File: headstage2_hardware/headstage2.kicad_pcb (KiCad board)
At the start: 6 copper layers, 113 parts, among them U1 OMNETICS_A79025, U10 TPS62410, U11 ABM10XTAL, U12 BF532-160, U13 NRF24L01, U14 MAX6711T, U15 SST25VF040B, U16 9x100, U17 ANTENNA, U18 9x100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

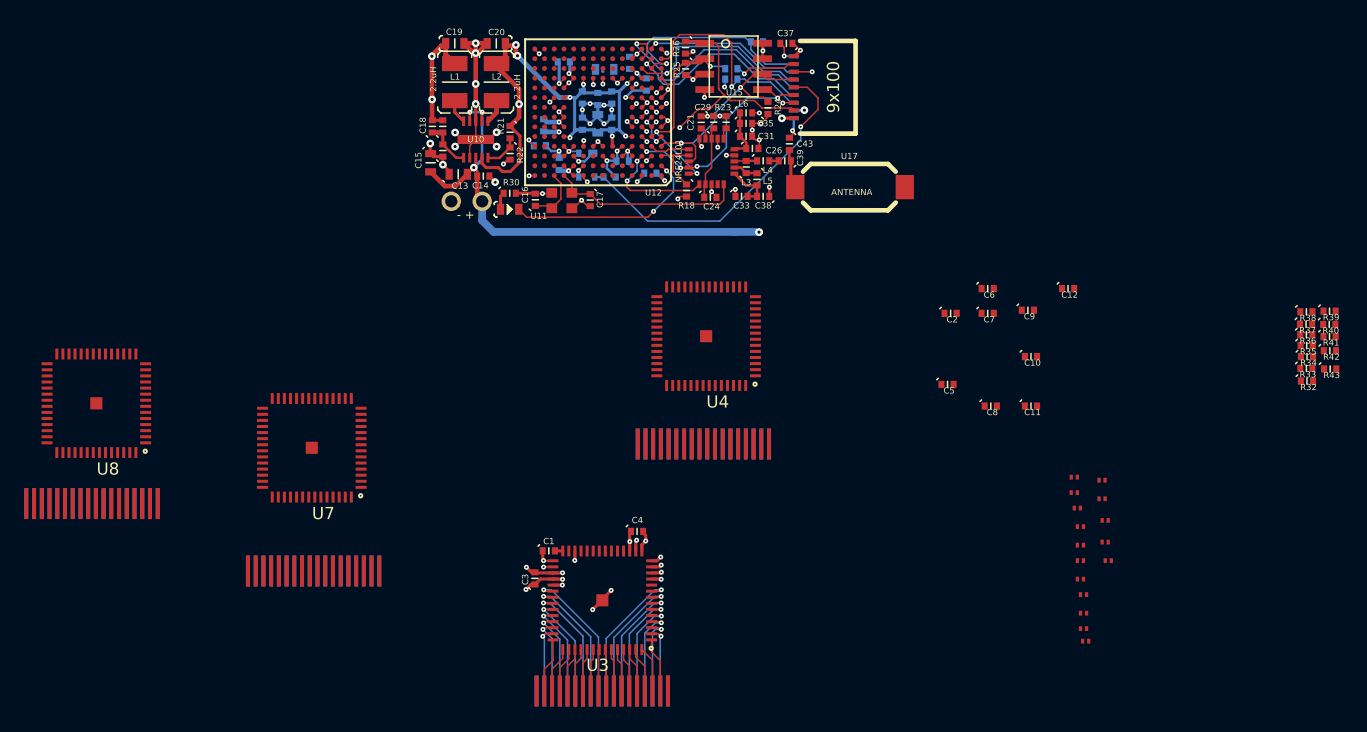
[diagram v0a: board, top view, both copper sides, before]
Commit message: Finished PCB layout, generated Gerber passed freedfm.com online check.
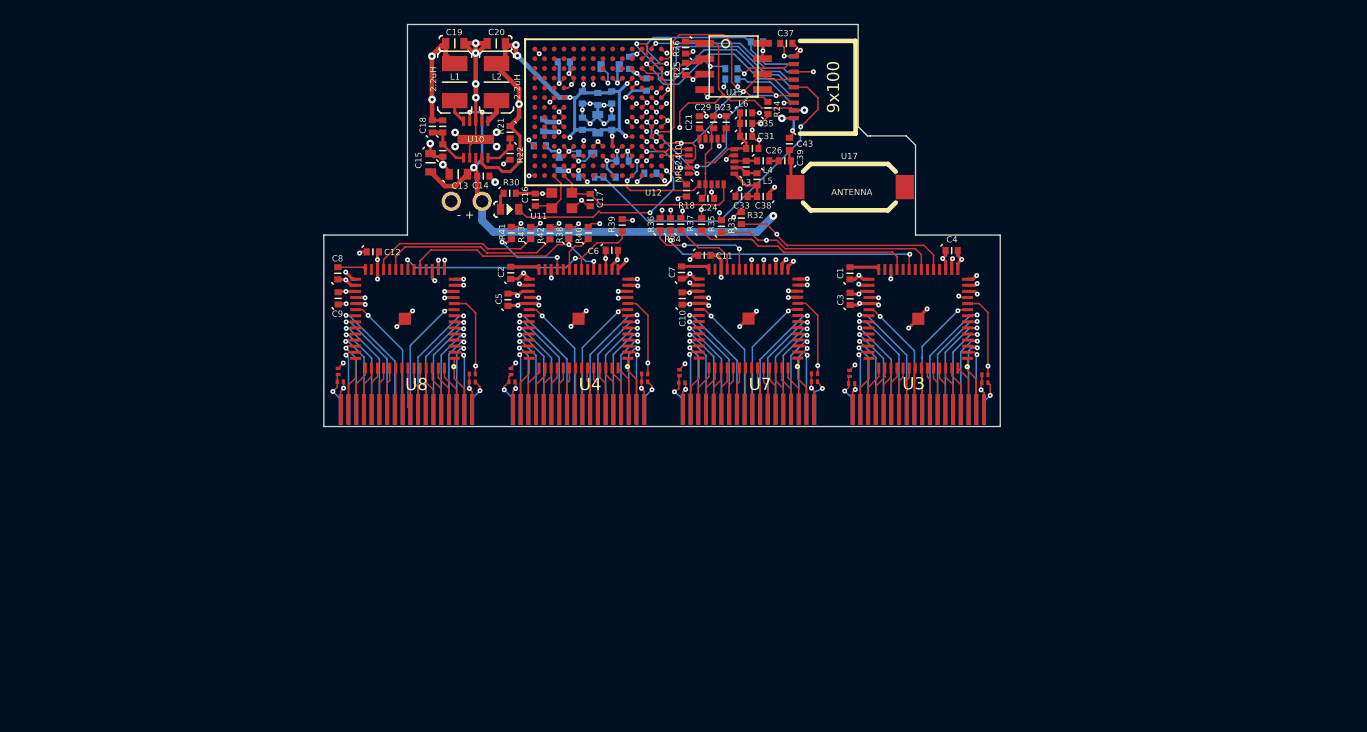
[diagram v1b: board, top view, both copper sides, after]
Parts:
- moved R41 67.8 mm to (129.5, 96.5), turned to 90 degrees
- moved R43 66.6 mm to (131.1, 96.5), turned to 90 degrees
- moved R16 65.2 mm to (115.3, 107.9), turned to 90 degrees
- moved R42 64.8 mm to (132.7, 96.5), turned to 90 degrees
- moved R14 63.9 mm to (115.5, 108.7)
- moved R40 61.4 mm to (135.8, 96.5), turned to 90 degrees
- moved R38 61.0 mm to (134.2, 96.5), turned to 90 degrees
- moved R39 58.6 mm to (138.6, 95.9), turned to 90 degrees
- moved C12 57.2 mm to (118.1, 98.1)
- moved C9 56.7 mm to (115.3, 101.9), turned to 90 degrees
- moved C8 54.8 mm to (115.2, 99.8), turned to 90 degrees
- moved R10 54.4 mm to (126.3, 108.1), turned to 180 degrees
- moved R36 53.9 mm to (141.7, 95.8), turned to 90 degrees
- moved R34 53.4 mm to (142.6, 95.8), turned to 90 degrees
- moved R12 52.4 mm to (126.3, 108.8), turned to 180 degrees
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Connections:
- C12 pad 1: Net-(C12-Pad1) -> GND
- R37 pad 1: /DROSEC_out -> /DR0SEC_out
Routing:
- net GND: track 214.3 -> 407.8 mm, vias 65 -> 105
- net VDD: track 126.4 -> 204.5 mm, vias 28 -> 46
- net /DT0PRI_out: track 0.00 -> 22.3 mm, vias 0 -> 2
- net /SCLK0_out: track 0.00 -> 21.5 mm, vias 0 -> 2
- net /FSync0_out: track 0.00 -> 21.5 mm, vias 0 -> 2
- net /SCLK1_out: track 0.00 -> 21.2 mm, vias 0 -> 2
- net Net-(R1-Pad1): track 0.00 -> 18.8 mm, vias 0 -> 2
- net Net-(R10-Pad1): track 0.00 -> 18.7 mm, vias 0 -> 2
- net Net-(R2-Pad1): track 0.00 -> 18.5 mm, vias 0 -> 2
- net Net-(R15-Pad2): track 0.00 -> 18.5 mm, vias 0 -> 2
- net /DR0PRI_out: track 0.00 -> 18.0 mm
- net /FSync1_out: track 0.00 -> 17.7 mm, vias 0 -> 2
- net /DT1SEC_out: track 0.00 -> 14.8 mm
- net /DR1SEC_out: track 0.00 -> 14.0 mm
- net /C_IN1: track 0.00 -> 10.5 mm, vias 0 -> 1
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- added copper zone on Inner2.ground, net GND
- added copper zone on Inner5.ground.sigs, net GND
- added copper zone on Inner3.VCC.sigs, net VCC
- added copper zone on Inner4.VDD, net VDD
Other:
- board outline added: 55.6 x 33 mm
- rule pad_to_mask_clearance: 0.2032 -> 0.0762

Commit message: Headstage2_hardware gerber gtkclient.cpp
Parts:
- R30: value 22K -> 200
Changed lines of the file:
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@@
     (links 486)
     (no_connects 0)
-    (area 114.086639 79.372459 169.694861 112.438181)
+    (area 113.403621 79.34706 169.939245 113.66754)
     (thickness 0.6858)
     (drawings 15)
@@
   )
   (setup
-    (last_trace_width 0.635)
+    (last_trace_width 0.127)
     (user_trace_width 0.127)
     (user_trace_width 0.2032)
@@
       (effects (font (size 0.508 0.508) (thickness 0.127)))
     )
-    (fp_text value 22K (at 0.127 -0.508) (layer F.SilkS) hide
-      (effects (font (size 0.508 0.508) (thickness 0.127)))
-    )
+    (fp_text value 200 (at 0.127 -0.508) (layer F.SilkS) hide
+      (effects (font (size 0.508 0.508) (thickness 0.127)))
+    )

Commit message: Found a mistake!!! My LED pad was put on the board backwards...the LED will always be reverse biased and not light up!
I've fixed this by changing the footprint associated with the LED,
changed the footprint on the PCB file, and updated the gerber and drill
file and SMD position files.
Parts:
- D1: footprint headstage2_library:D0603 -> D0603
- moved D1 0.10 mm to (129.4, 94.7), turned to 180 degrees
